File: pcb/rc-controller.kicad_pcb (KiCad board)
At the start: 2 copper layers, 153.4 x 76.2 mm, 79 parts, among them J2 USB_C_Receptacle_USB2.0_16P, M1 Motor_DC, Q1 AO3401A, Q2 AO3401A, Q3 AO3400A, Q4 AO3400A, SW1 SW_SPDT, SW2 SW_SPDT, SW3 SW_Push, SW4 SW_Push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

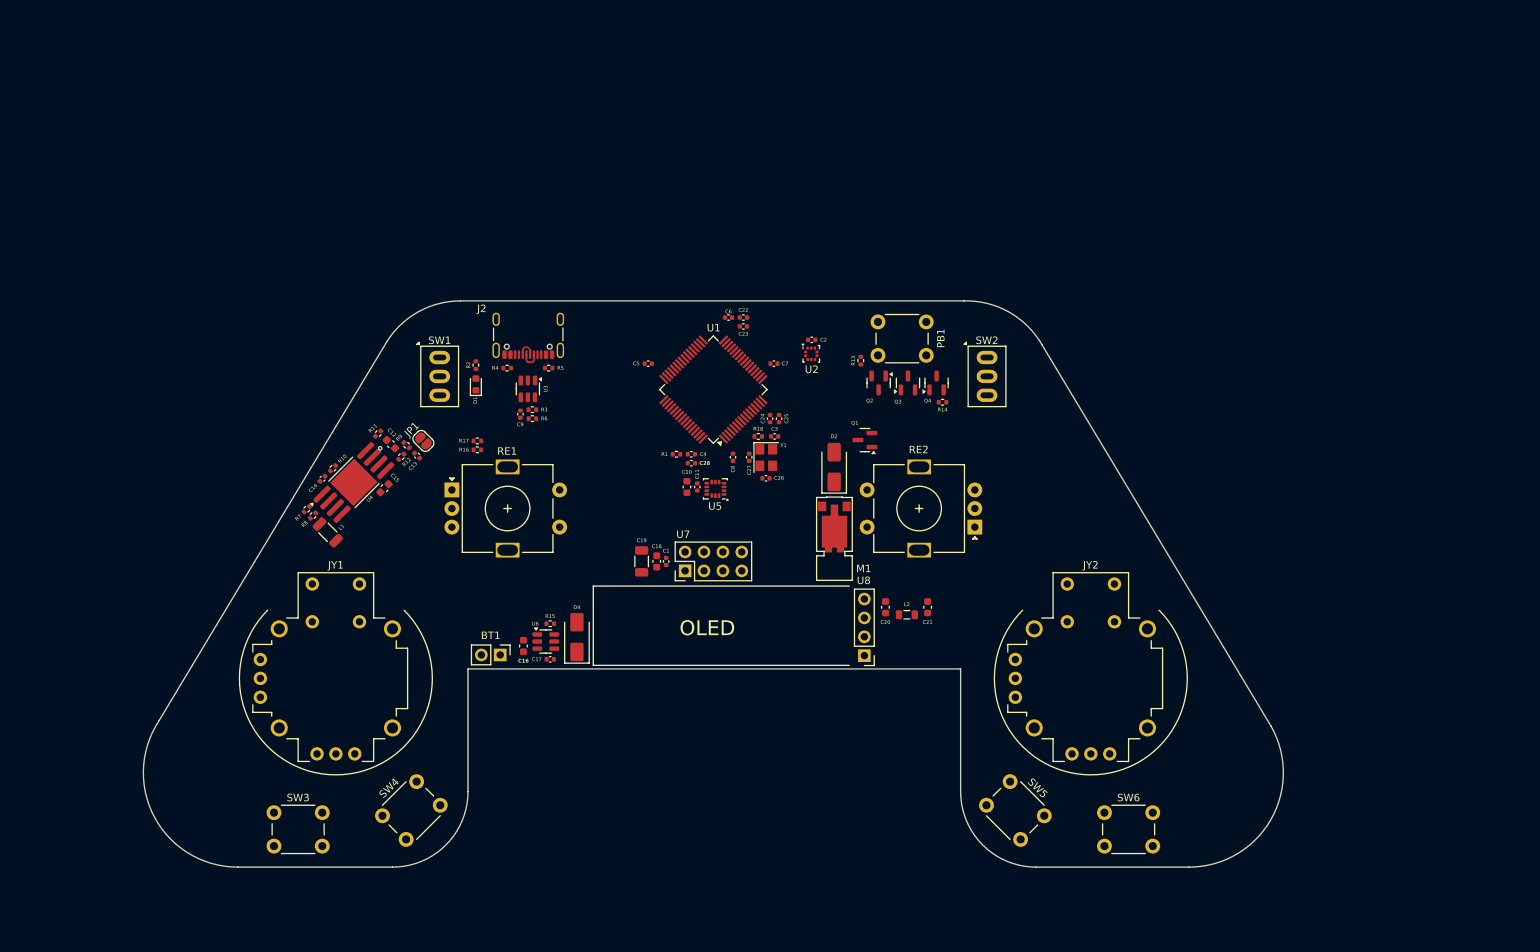
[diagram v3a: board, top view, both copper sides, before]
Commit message: Finish schematic
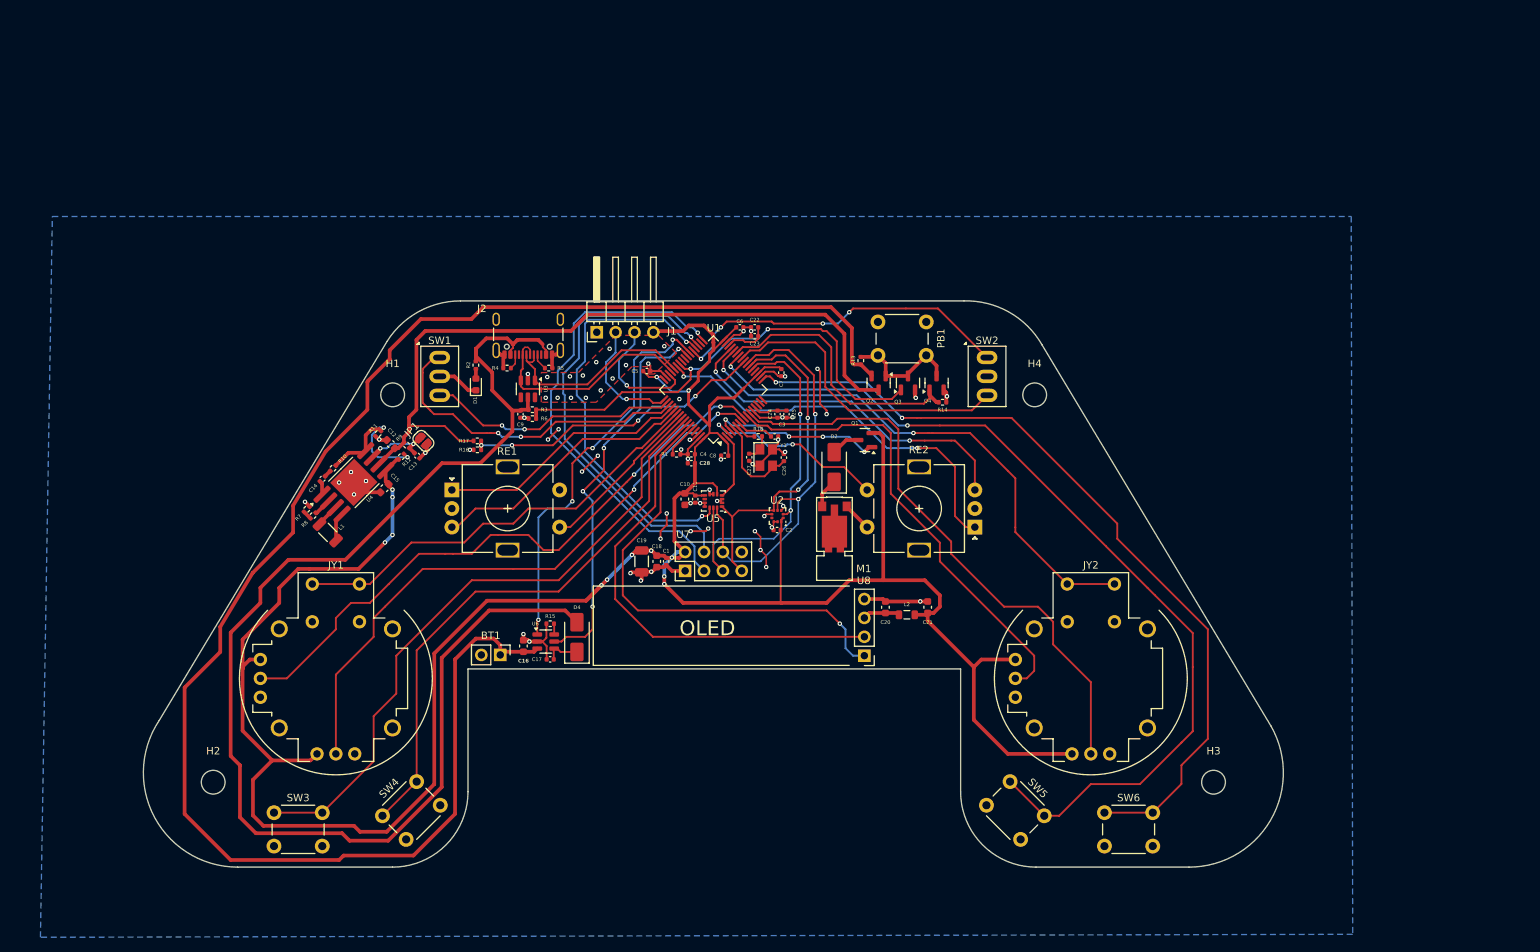
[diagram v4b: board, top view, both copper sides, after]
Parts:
- added H1: MountingHole, MountingHole:MountingHole_3.2mm_M3, F.Cu at (94.0, 73.6)
- added H2: MountingHole, MountingHole:MountingHole_3.2mm_M3, F.Cu at (69.8, 125.7)
- added H3: MountingHole, MountingHole:MountingHole_3.2mm_M3, F.Cu at (204.5, 125.7)
- added H4: MountingHole, MountingHole:MountingHole_3.2mm_M3, F.Cu at (180.4, 73.6)
- added J1: Conn_01x04_Pin, Connector_PinHeader_2.54mm:PinHeader_1x04_P2.54mm_Horizontal, F.Cu at (121.5, 65.2)
- moved C2 26.0 mm to (145.7, 91.8), turned to 180 degrees
- moved U2 22.3 mm to (145.8, 89.9), turned to 180 degrees
- moved C26 3.68 mm to (146.6, 82.0), turned to -90 degrees
- moved C22 2.01 mm to (142.7, 64.5)
- moved C6 2.01 mm to (140.7, 64.5)
- moved C23 2.01 mm to (142.7, 65.7)
- moved C10 1.66 mm to (133.3, 87.6)
- moved C11 1.66 mm to (134.7, 87.6)
- moved U5 1.66 mm to (137.2, 87.9)
- moved C7 1.56 mm to (146.3, 70.6), turned to -90 degrees
- moved C25 1.16 mm to (147.0, 76.2)
- moved C24 1.16 mm to (145.8, 76.2)
- moved C8 1.14 mm to (138.7, 81.8), turned to 180 degrees
- moved C5 1.02 mm to (128.2, 70.4)
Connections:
- net /OSCIN renamed /XTALH
- net /OSCLO renamed /XTALC
- net /OSCOUT renamed /XTALL
- JY1 pad B1: GND -> /JY1SW
- JY1 pad H1: (no net) -> +3V3
- JY1 pad H2: (no net) -> /JY1Y
- JY1 pad H3: (no net) -> GND
- JY1 pad S1: /JY1SW -> GND
- JY1 pad V1: (no net) -> +3V3
- JY1 pad V2: (no net) -> /JY1X
- JY1 pad V3: (no net) -> GND
- JY2 pad B1: GND -> /JY2SW
- JY2 pad H1: (no net) -> +3V3
- JY2 pad H2: (no net) -> /JY2Y
- JY2 pad H3: (no net) -> GND
- JY2 pad S1: /JY2SW -> GND
- JY2 pad V1: (no net) -> +3V3
- JY2 pad V2: (no net) -> /JY2X
- JY2 pad V3: (no net) -> GND
- Q4 pad 1: /PWRON -> /BON
- R14 pad 1: /PWRON -> /BON
- SW1 pad 1: /TSW1A -> /SW1A
- SW1 pad 3: /TSW1B -> /SW1B
- SW2 pad 1: /TSW2A -> /SW2A
- SW2 pad 3: /TSW2B -> /SW2B
- SW3 pad 1: /BT1 -> /BTN1
- SW4 pad 1: /BT2 -> /BTN2
- SW5 pad 1: /BT3 -> /BTN3
- SW6 pad 1: /BT4 -> /BTN4
- U1 pad 10: unconnected-(U1-PC2-Pad10) -> /JY2X
- U1 pad 11: unconnected-(U1-PC3-Pad11) -> /JY2Y
- U1 pad 17: unconnected-(U1-PA3-Pad17) -> /BTN4
- U1 pad 2: unconnected-(U1-PC13-Pad2) -> /GINT1
- U1 pad 21: unconnected-(U1-PA5-Pad21) -> /SNCLK
- U1 pad 22: unconnected-(U1-PA6-Pad22) -> /SNMISO
- U1 pad 23: unconnected-(U1-PA7-Pad23) -> /SNMOSI
- U1 pad 24: unconnected-(U1-PC4-Pad24) -> /BREF
- U1 pad 25: unconnected-(U1-PC5-Pad25) -> /SW2B
- U1 pad 26: unconnected-(U1-PB0-Pad26) -> /BTN3
- U1 pad 27: unconnected-(U1-PB1-Pad27) -> /BON
- U1 pad 28: unconnected-(U1-PB2-Pad28) -> /JY2SW
- U1 pad 29: unconnected-(U1-PB10-Pad29) -> /RE2B
- U1 pad 3: unconnected-(U1-PC14-Pad3) -> /RE2SW
- U1 pad 33: unconnected-(U1-PB12-Pad33) -> /RFCE
- U1 pad 35: unconnected-(U1-PB14-Pad35) -> /RFCS
- U1 pad 36: unconnected-(U1-PB15-Pad36) -> /GCS
- U1 pad 37: unconnected-(U1-PC6-Pad37) -> /SW2A
- U1 pad 38: unconnected-(U1-PC7-Pad38) -> /CHRG
- U1 pad 39: unconnected-(U1-PC8-Pad39) -> /STDBY
- U1 pad 4: unconnected-(U1-PC15-Pad4) -> /MTR
- U1 pad 43: unconnected-(U1-PA10-Pad43) -> /RE2A
- U1 pad 46: unconnected-(U1-PA13-Pad46) -> /SWDIO
- U1 pad 49: unconnected-(U1-PA14-Pad49) -> /SWCLK
- U1 pad 50: unconnected-(U1-PA15-Pad50) -> /SW1B
- U1 pad 51: unconnected-(U1-PC10-Pad51) -> /SW1A
- U1 pad 52: unconnected-(U1-PC11-Pad52) -> /RE1A
- U1 pad 53: unconnected-(U1-PC12-Pad53) -> /RE1B
- U1 pad 54: unconnected-(U1-PD2-Pad54) -> /JY1SW
- U1 pad 55: unconnected-(U1-PB3-Pad55) -> /RE1SW
- U1 pad 56: unconnected-(U1-PB4-Pad56) -> /BTN1
- U1 pad 57: unconnected-(U1-PB5-Pad57) -> /BTN2
- U1 pad 58: unconnected-(U1-PB6-Pad58) -> /SCL
- U1 pad 59: unconnected-(U1-PB7-Pad59) -> /SDA
- U1 pad 62: unconnected-(U1-PB9-Pad62) -> /PCS
- U1 pad 8: unconnected-(U1-PC0-Pad8) -> /JY1Y
- U1 pad 9: unconnected-(U1-PC1-Pad9) -> /JY1X
- U2 pad 2: /SNSCK -> /SNCLK
- U2 pad 7: /DRDY -> unconnected-(U2-INT_DRDY-Pad7)
- U5 pad 13: /SNSCK -> /SNCLK
- U5 pad 4: /GINT1 -> unconnected-(U5-INT1-Pad4)
- U7 pad 5: /RFSCK -> /SNCLK
- U7 pad 6: /RFMOSI -> /SNMOSI
- U7 pad 7: /RFMISO -> /SNMISO
- U7 pad 8: /RFIRQ -> unconnected-(U7-IRQ-Pad8)
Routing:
- net +3V3: track 0.00 -> 372.7 mm, vias 0 -> 13
- net VBATT: track 0.00 -> 223.1 mm
- net VBUS: track 0.00 -> 178.3 mm
- net GND: track 0.00 -> 123.7 mm, vias 0 -> 65
- net /BTN3: track 0.00 -> 123.4 mm, vias 0 -> 2
- net /BTN4: track 0.00 -> 109.6 mm, vias 0 -> 2
- net VPWR: track 0.00 -> 99.7 mm
- net /BTN1: track 0.00 -> 86.5 mm
- net /JY1X: track 0.00 -> 83.5 mm, vias 0 -> 2
- net /JY1Y: track 0.00 -> 82.0 mm, vias 0 -> 2
- net /JY2Y: track 0.00 -> 78.6 mm
- net /BTN2: track 0.00 -> 76.6 mm
- net /JY2SW: track 0.00 -> 72.0 mm, vias 0 -> 2
- net /RFCE: track 0.00 -> 65.2 mm, vias 0 -> 1
- net /SNSBUS: track 0.00 -> 64.9 mm, vias 0 -> 2
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- added copper zone on B.Cu, net GND
- added copper zone on F.Cu, net GND

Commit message: Finish layout
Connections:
- U1 pad 2: /GINT1 -> unconnected-(U1-PC13-Pad2)
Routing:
- net /PCS: track 2.55 -> 17.0 mm
- net /GINT1: track 9.07 -> 0.00 mm
- net GND: track 123.7 -> 127.9 mm, vias 65 -> 67
- net +3V3: vias 13 -> 10

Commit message: Add silkscreen
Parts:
- added G1: Monkey, LOGO, B.Cu at (179.8, 106.9)
- added G2: Engine, LOGO, B.Cu at (137.2, 92.2)
- added G3: GROOT, LOGO, B.Cu at (90.2, 108.5)
- moved R7 0.21 mm to (82.3, 89.2)
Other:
- board text added: "B+"
- board text added: "Designed By: Miguel Flores-Acton"
- board text added: "GND"
- board text added: "RF Remote V1.0"

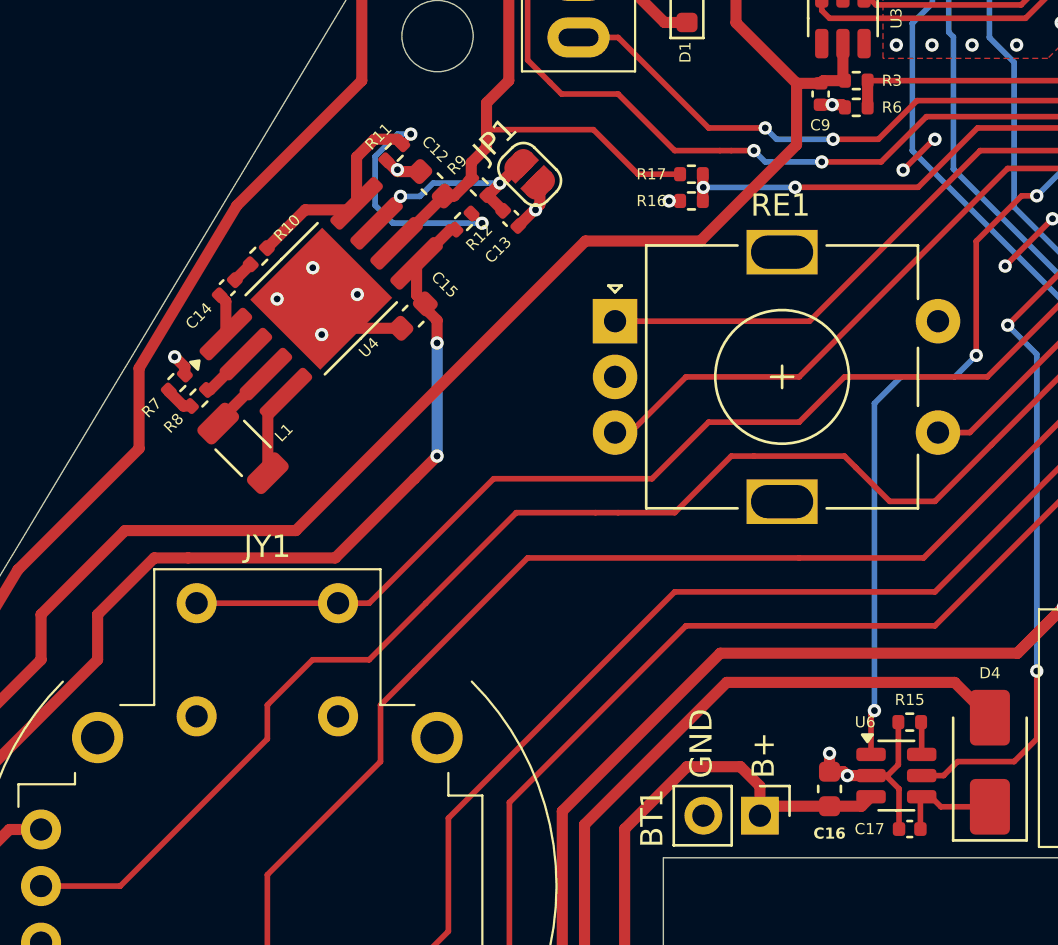
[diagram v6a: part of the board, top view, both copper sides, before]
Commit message: Fix bom and generate fab files
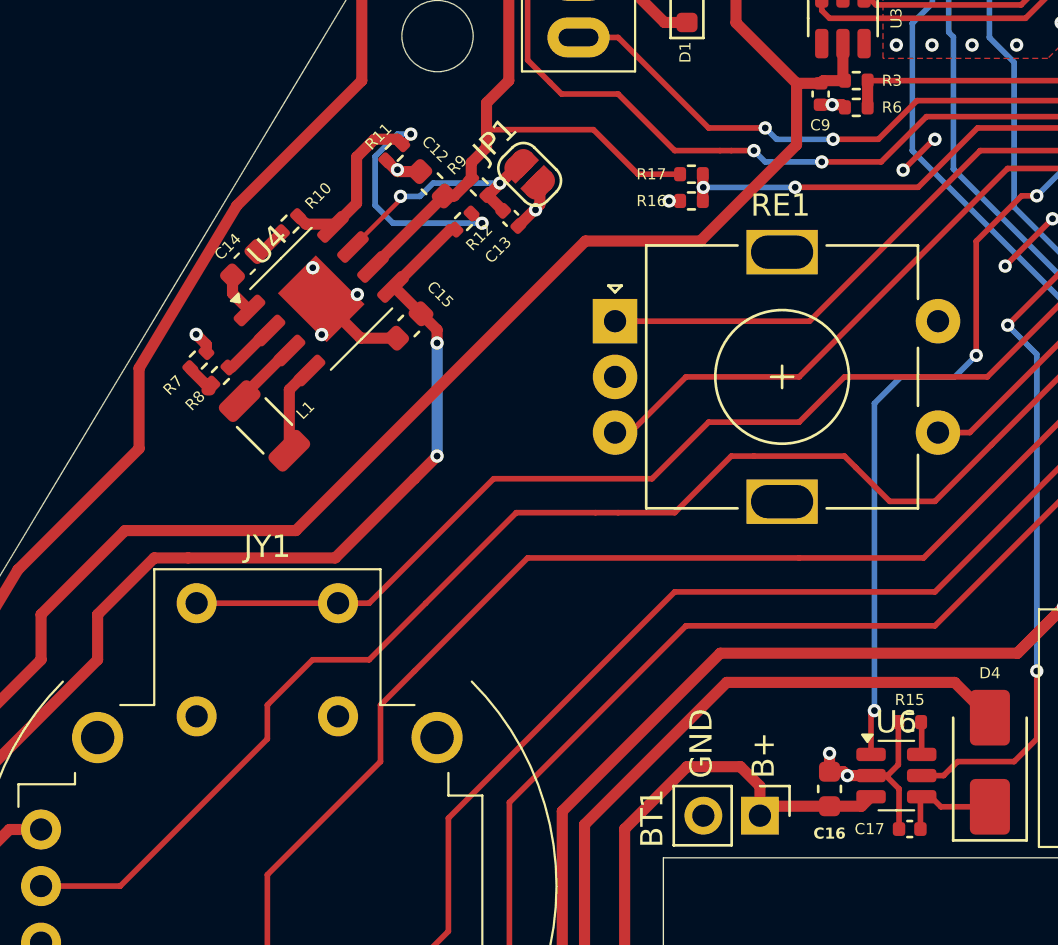
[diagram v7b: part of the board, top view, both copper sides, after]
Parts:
- C14: footprint Capacitor_SMD:C_0402_1005Metric -> Capacitor_SMD:C_0603_1608Metric
- R12: value 340k -> 330k
- R9: value 1m -> 1M
- U4: footprint Package_SO:SOP-8-1EP_4.57x4.57mm_P1.27mm_EP4.57x4.45mm -> Package_SO:HSOP-8-1EP_3.9x4.9mm_P1.27mm_EP2.41x3.1mm
- U6: footprint Package_TO_SOT_SMD:TSOT-23-6 -> Package_TO_SOT_SMD:SOT-23-6
- moved R10 2.01 mm to (87.4, 82.0)
- moved R8 1.40 mm to (84.3, 88.8)
- moved R7 1.40 mm to (83.3, 88.1)
- moved L1 1.40 mm to (86.2, 91.1)
- moved C14 1.33 mm to (85.3, 83.8)
- moved C15 0.48 mm to (92.7, 86.6)
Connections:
- M1 pad SH: (no net) -> unconnected-(M1-PadSH)_1
- RE1 pad MP: (no net) -> GND
- RE2 pad MP: (no net) -> GND
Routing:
- net Net-(U4-FB): track 20.1 -> 18.4 mm
- net VPWR: track 99.7 -> 101.2 mm
- net Net-(JP1-B): track 9.41 -> 10.9 mm
- net +3V3: track 372.7 -> 373.6 mm
- net GND: vias 67 -> 66

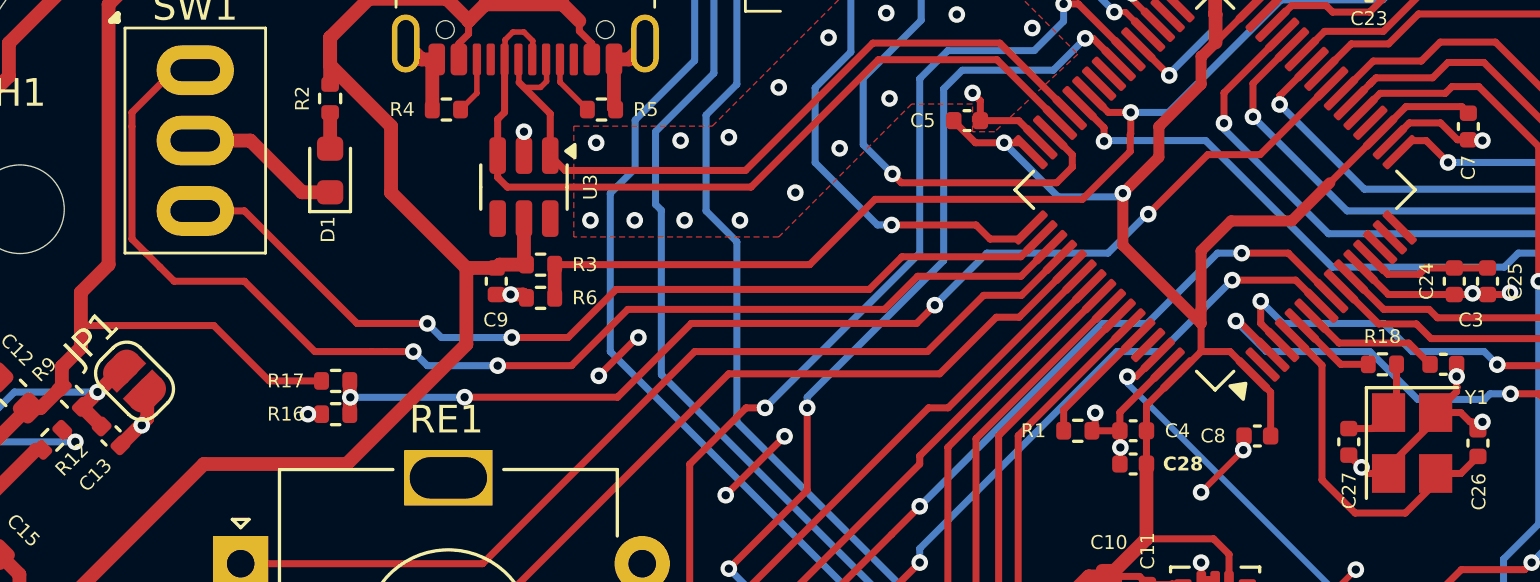
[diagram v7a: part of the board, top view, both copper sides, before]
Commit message: Initialize stm32 project and fix vref issue
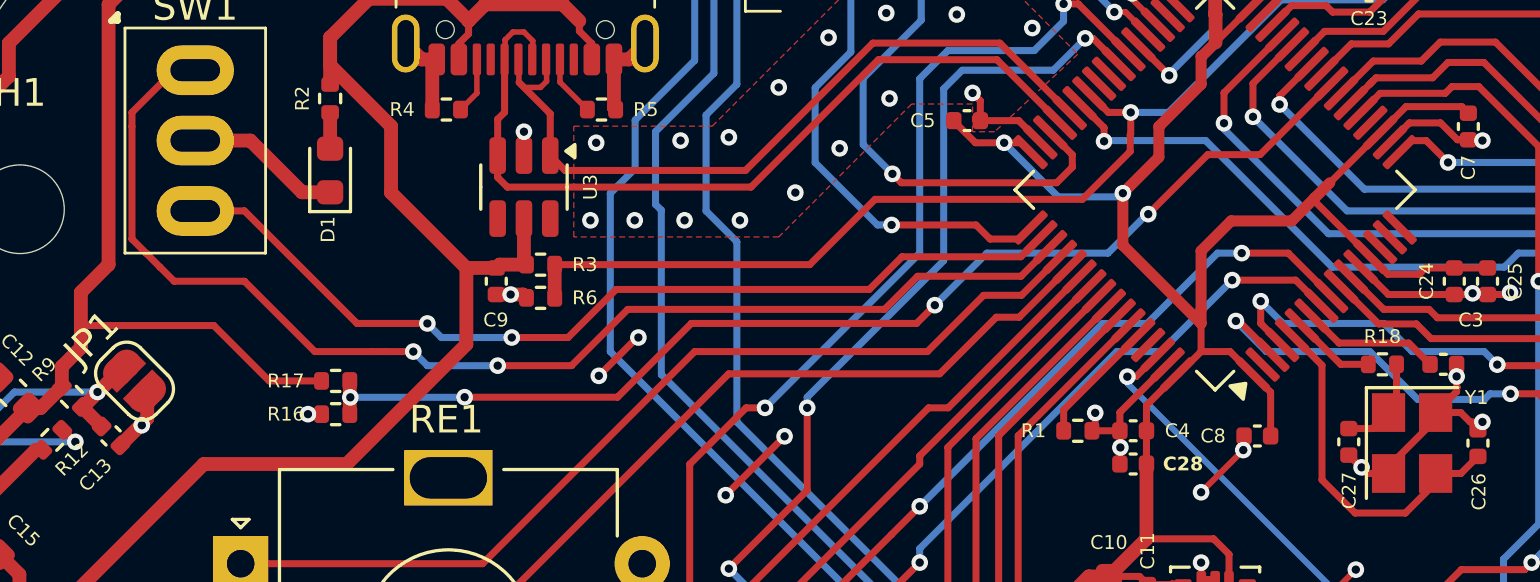
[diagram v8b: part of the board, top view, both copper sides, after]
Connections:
- C24 pad 1: /VREF -> +3V3
- C25 pad 1: /VREF -> +3V3
- U1 pad 13: /VREF -> +3V3
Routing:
- net +3V3: track 373.6 -> 381.2 mm
- net /VREF: track 4.59 -> 0.00 mm
